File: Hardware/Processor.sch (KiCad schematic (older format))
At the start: 31 parts, among them J1 ICSP-CORTEX, J3 CONN-9, U6 STM32L100RBT6, U9 LM2903DT, X1 8MHz

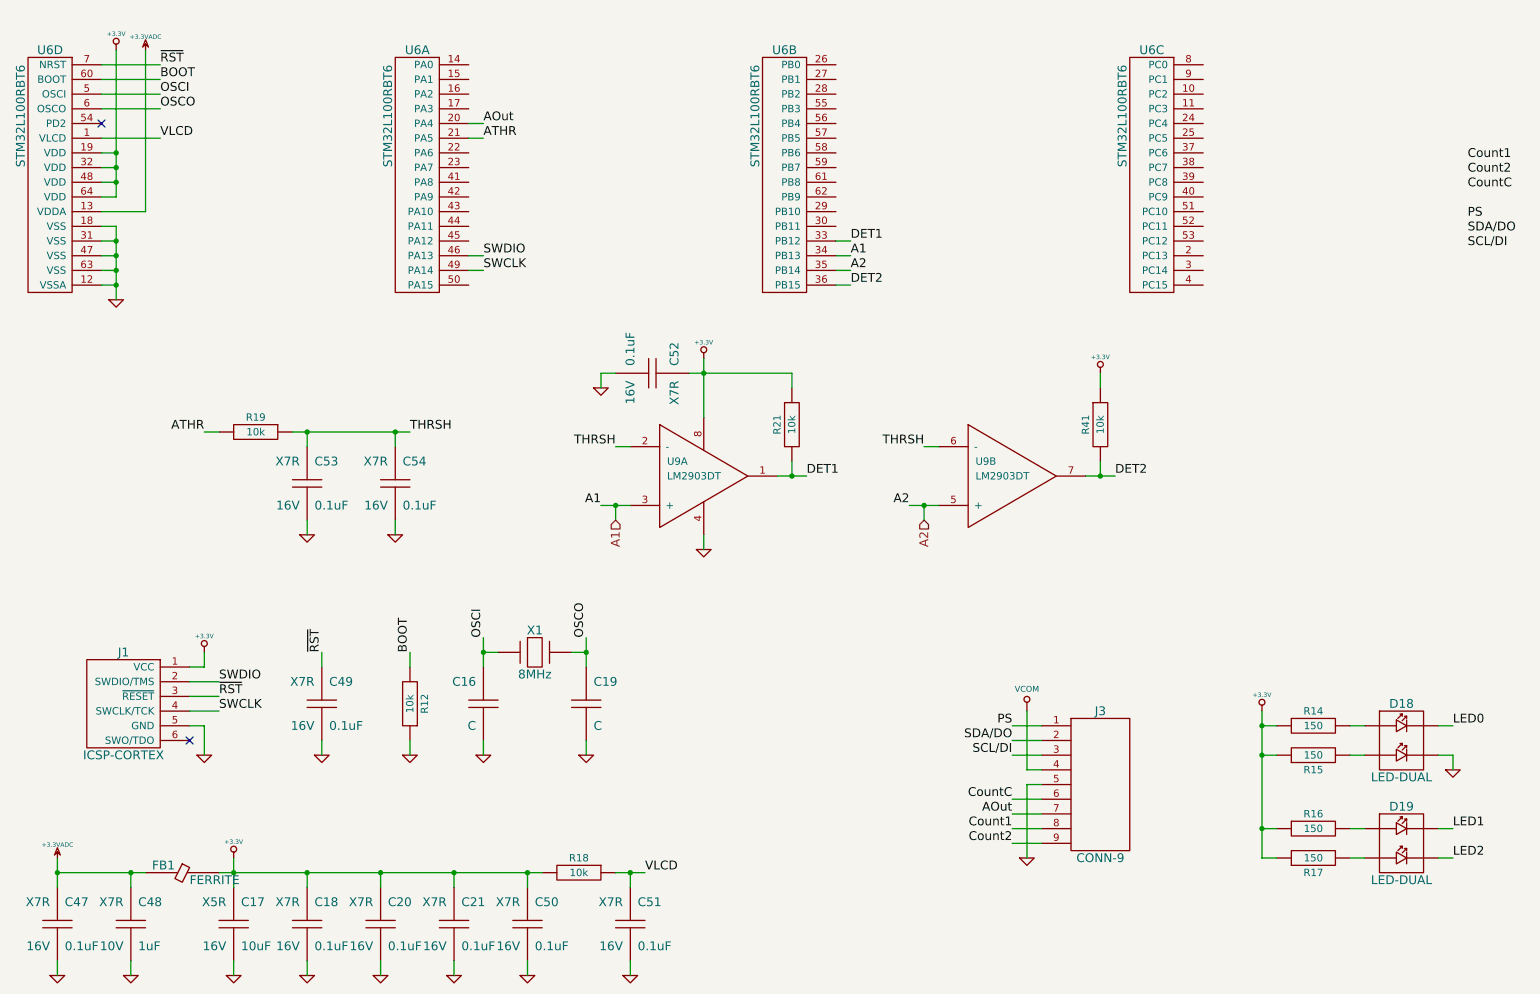
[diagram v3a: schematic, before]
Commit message: Serial IO connections
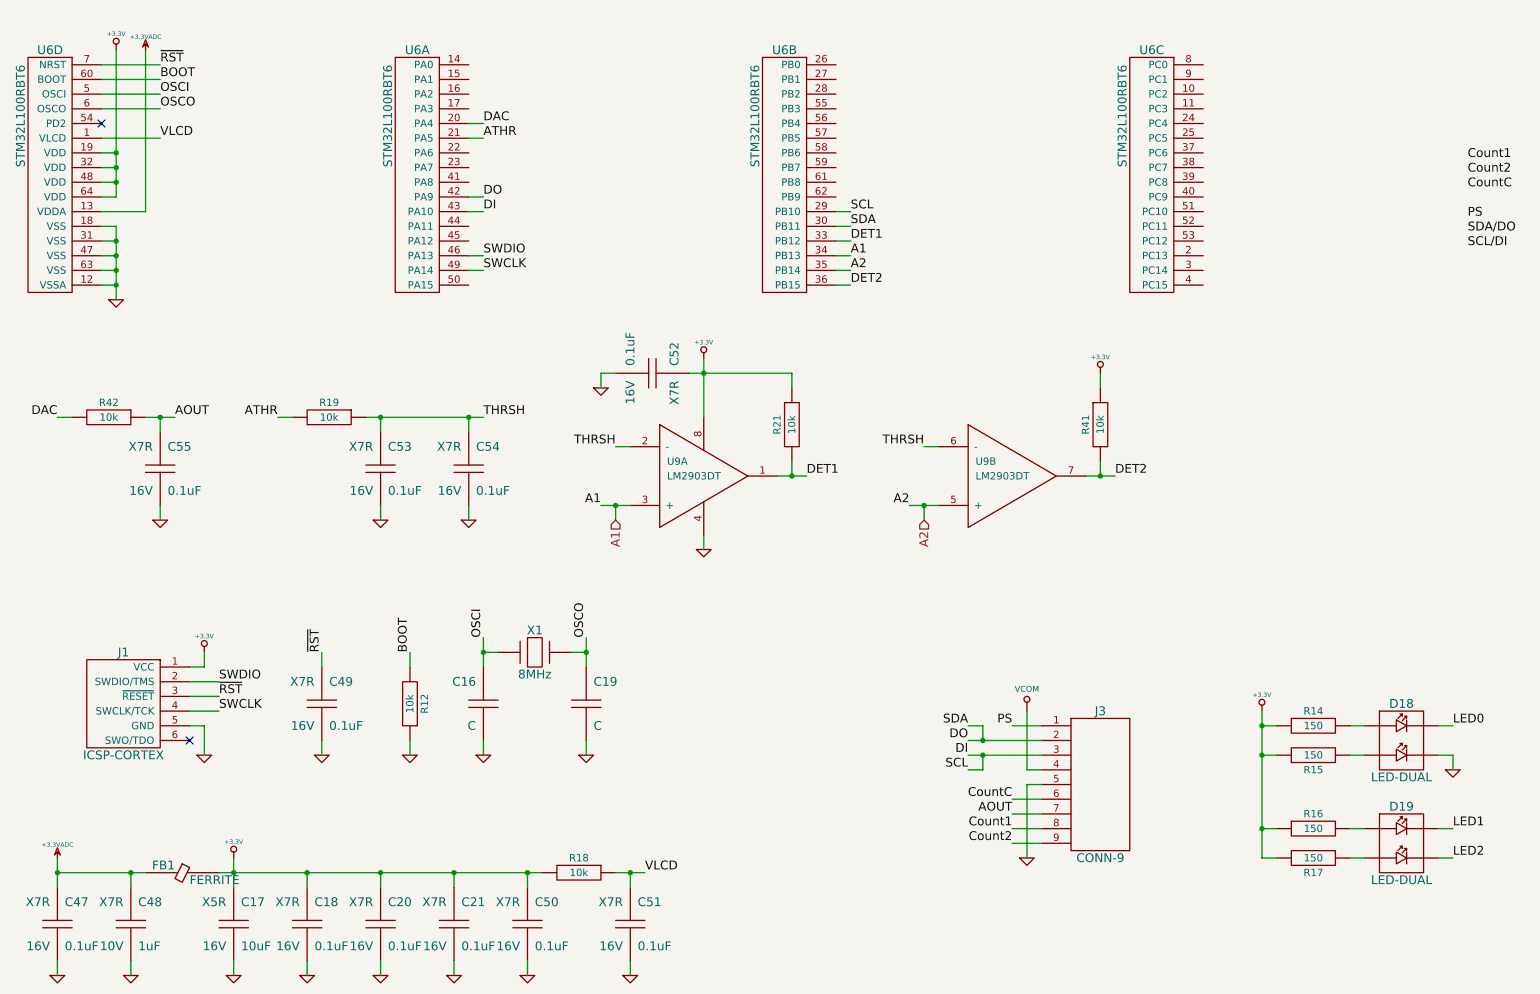
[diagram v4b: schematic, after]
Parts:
- added C55: 0.1uF, CAPC1608, symbol C
- added R42: 10k, RESC1608, symbol R
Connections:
- net GND: now also C55.2
- net SCL/DI: no longer J3.3
- net SDA/DO: no longer J3.2
- net DO: now reaches U6.42 (PA9)
- net DO: now also J3.2, U6.30 (PB11)
- net DI: now reaches U6.43 (PA10)
- net DI: now also J3.3, U6.29 (PB10)
- net AOut renamed AOUT
- net AOUT: now also C55.1, R42.1; no longer U6.20 (PA4)
- new net DAC: R42.2, U6.20 (PA4)
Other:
- moved on the sheet: C53, C54, R19
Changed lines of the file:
@@
 $EndComp
 $Comp
-L VCOM #PWR56
+L VCOM #PWR57
 U 1 1 52B50CC7
 P 7700 5400
-F 0 "#PWR56" H 7700 5600 40  0001 C CNN
+F 0 "#PWR57" H 7700 5600 40  0001 C CNN
 F 1 "VCOM" H 7700 5550 40  0000 C CNN
 F 2 "" H 7700 5400 60  0000 C CNN
@@
 	1    0    0    -1
 $EndComp
-Text Label 7600 5600 2    60   ~ 0
-SDA/DO
-Text Label 7600 5700 2    60   ~ 0
-SCL/DI
+Text Label 7300 5600 2    60   ~ 0
+DO
+Text Label 7300 5700 2    60   ~ 0
+DI
 $Comp
 L LED-DUAL D18
@@
 	7700 5800 7800 5800
 Wire Wire Line
-	7600 5600 7800 5600
-Wire Wire Line
-	7600 5700 7800 5700
+	7300 5600 7800 5600
+Wire Wire Line
+	7300 5700 7800 5700
 Wire Wire Line
 	10600 5800 10600 5700
@@
 	7600 5500 7800 5500
 Text Label 7600 6100 2    60   ~ 0
-AOut
+AOUT
 Wire Wire Line
 	7600 6100 7800 6100
@@
 CountC
 Text Label 4000 1400 0    60   ~ 0
-AOut
+DAC
 Text Label 10700 2050 0    60   ~ 0
 PS
@@
 Wire Wire Line
 	8200 3100 8200 3200
-Text Label 3500 3500 0    60   ~ 0
+Text Label 4000 3400 0    60   ~ 0
 THRSH
-Text Label 2100 3500 2    60   ~ 0
+Text Label 2600 3400 2    60   ~ 0
 ATHR
 Wire Wire Line
-	2100 3500 2200 3500
-Wire Wire Line
-	2700 3500 3500 3500
-Wire Wire Line
-	2800 3600 2800 3500
-Connection ~ 2800 3500
+	2600 3400 2700 3400
+Wire Wire Line
+	3200 3400 4000 3400
+Wire Wire Line
+	3300 3500 3300 3400
+Connection ~ 3300 3400
 $Comp
 L GND #PWR058
 U 1 1 54120E8C
-P 2800 4200
-F 0 "#PWR058" H 2800 4200 30  0001 C CNN
-F 1 "GND" H 2800 4130 30  0001 C CNN
-F 2 "" H 2800 4200 60  0000 C CNN
-F 3 "" H 2800 4200 60  0000 C CNN
-	1    2800 4200
-	1    0    0    -1
-$EndComp
-Wire Wire Line
-	2800 4200 2800 4100
+P 3300 4100
+F 0 "#PWR058" H 3300 4100 30  0001 C CNN
+F 1 "GND" H 3300 4030 30  0001 C CNN
+F 2 "" H 3300 4100 60  0000 C CNN
+F 3 "" H 3300 4100 60  0000 C CNN
+	1    3300 4100
+	1    0    0    -1
+$EndComp
+Wire Wire Line
+	3300 4100 3300 4000
 $Comp
 L C C53
 U 1 1 54120F9B
-P 2800 3850
-F 0 "C53" H 2850 4000 60  0000 L CNN
-F 1 "0.1uF" H 2850 3700 60  0000 L CNN
-F 2 "CAPC1608" H 2800 3850 60  0001 C CNN
-F 3 "~" H 2800 3850 60  0000 C CNN
-F 4 "Samsung" H 2800 3850 60  0001 C CNN "MFR Name"
-F 5 "CL10B104KO8NNNC" H 2800 3850 60  0001 C CNN "MFR Part No"
-F 6 "1276-1005-1-ND" H 2800 3850 60  0001 C CNN "Distributor Part No"
-F 7 "16V" H 2750 3700 60  0000 R CNN "Voltage"
-F 8 "X7R" H 2750 4000 60  0000 R CNN "Dielectric"
-	1    2800 3850
+P 3300 3750
+F 0 "C53" H 3350 3900 60  0000 L CNN
+F 1 "0.1uF" H 3350 3600 60  0000 L CNN
+F 2 "CAPC1608" H 3300 3750 60  0001 C CNN
+F 3 "~" H 3300 3750 60  0000 C CNN
+F 4 "Samsung" H 3300 3750 60  0001 C CNN "MFR Name"
+F 5 "CL10B104KO8NNNC" H 3300 3750 60  0001 C CNN "MFR Part No"
+F 6 "1276-1005-1-ND" H 3300 3750 60  0001 C CNN "Distributor Part No"
+F 7 "16V" H 3250 3600 60  0000 R CNN "Voltage"
+F 8 "X7R" H 3250 3900 60  0000 R CNN "Dielectric"
+	1    3300 3750
 	1    0    0    -1
 $EndComp
@@
 L R R19
 U 1 1 54120FD3
-P 2450 3500
-F 0 "R19" H 2450 3600 50  0000 C CNN
-F 1 "10k" H 2450 3500 50  0000 C CNN
-F 2 "RESC1608" H 2450 3500 60  0001 C CNN
-F 3 "~" H 2450 3500 60  0000 C CNN
-F 4 "Yageo" H 2450 3500 60  0001 C CNN "MFR Name"
-F 5 "RC0603FR-0710KL" H 2450 3500 60  0001 C CNN "MFR Part No"
-F 6 "311-10.0KHRCT-ND" H 2450 3500 60  0001 C CNN "Distributor Part No"
-F 7 "0.1W" H 2450 3400 50  0001 C CNN "Power"
-F 8 "1%" H 2450 3300 50  0001 C CNN "Tolerance"
-	1    2450 3500
+P 2950 3400
+F 0 "R19" H 2950 3500 50  0000 C CNN
+F 1 "10k" H 2950 3400 50  0000 C CNN
+F 2 "RESC1608" H 2950 3400 60  0001 C CNN
+F 3 "~" H 2950 3400 60  0000 C CNN
+F 4 "Yageo" H 2950 3400 60  0001 C CNN "MFR Name"
+F 5 "RC0603FR-0710KL" H 2950 3400 60  0001 C CNN "MFR Part No"
+F 6 "311-10.0KHRCT-ND" H 2950 3400 60  0001 C CNN "Distributor Part No"
+F 7 "0.1W" H 2950 3300 50  0001 C CNN "Power"
+F 8 "1%" H 2950 3200 50  0001 C CNN "Tolerance"
+	1    2950 3400
 	-1   0    0    -1
 $EndComp
@@
 L C C54
 U 1 1 541211F5
-P 3400 3850
-F 0 "C54" H 3450 4000 60  0000 L CNN
-F 1 "0.1uF" H 3450 3700 60  0000 L CNN
-F 2 "CAPC1608" H 3400 3850 60  0001 C CNN
-F 3 "~" H 3400 3850 60  0000 C CNN
-F 4 "Samsung" H 3400 3850 60  0001 C CNN "MFR Name"
-F 5 "CL10B104KO8NNNC" H 3400 3850 60  0001 C CNN "MFR Part No"
-F 6 "1276-1005-1-ND" H 3400 3850 60  0001 C CNN "Distributor Part No"
-F 7 "16V" H 3350 3700 60  0000 R CNN "Voltage"
-F 8 "X7R" H 3350 4000 60  0000 R CNN "Dielectric"
-	1    3400 3850
-	1    0    0    -1
-$EndComp
-Wire Wire Line
-	3400 3600 3400 3500
-Connection ~ 3400 3500
+P 3900 3750
+F 0 "C54" H 3950 3900 60  0000 L CNN
+F 1 "0.1uF" H 3950 3600 60  0000 L CNN
+F 2 "CAPC1608" H 3900 3750 60  0001 C CNN
+F 3 "~" H 3900 3750 60  0000 C CNN
+F 4 "Samsung" H 3900 3750 60  0001 C CNN "MFR Name"
+F 5 "CL10B104KO8NNNC" H 3900 3750 60  0001 C CNN "MFR Part No"
+F 6 "1276-1005-1-ND" H 3900 3750 60  0001 C CNN "Distributor Part No"
+F 7 "16V" H 3850 3600 60  0000 R CNN "Voltage"
+F 8 "X7R" H 3850 3900 60  0000 R CNN "Dielectric"
+	1    3900 3750
+	1    0    0    -1
+$EndComp
+Wire Wire Line
+	3900 3500 3900 3400
+Connection ~ 3900 3400
 $Comp
 L GND #PWR059
 U 1 1 541212A0
-P 3400 4200
-F 0 "#PWR059" H 3400 4200 30  0001 C CNN
-F 1 "GND" H 3400 4130 30  0001 C CNN
-F 2 "" H 3400 4200 60  0000 C CNN
-F 3 "" H 3400 4200 60  0000 C CNN
-	1    3400 4200
-	1    0    0    -1
-$EndComp
-Wire Wire Line
-	3400 4200 3400 4100
+P 3900 4100
+F 0 "#PWR059" H 3900 4100 30  0001 C CNN
+F 1 "GND" H 3900 4030 30  0001 C CNN
+F 2 "" H 3900 4100 60  0000 C CNN
+F 3 "" H 3900 4100 60  0000 C CNN
+	1    3900 4100
+	1    0    0    -1
+$EndComp
+Wire Wire Line
+	3900 4100 3900 4000
+$Comp
+L R R42
+U 1 1 54121756
+P 1450 3400
+F 0 "R42" H 1450 3500 50  0000 C CNN
+F 1 "10k" H 1450 3400 50  0000 C CNN
+F 2 "RESC1608" H 1450 3400 60  0001 C CNN
+F 3 "~" H 1450 3400 60  0000 C CNN
+F 4 "Yageo" H 1450 3400 60  0001 C CNN "MFR Name"
+F 5 "RC0603FR-0710KL" H 1450 3400 60  0001 C CNN "MFR Part No"
+F 6 "311-10.0KHRCT-ND" H 1450 3400 60  0001 C CNN "Distributor Part No"
+F 7 "0.1W" H 1450 3300 50  0001 C CNN "Power"
+F 8 "1%" H 1450 3200 50  0001 C CNN "Tolerance"
+	1    1450 3400
+	-1   0    0    -1
+$EndComp
+$Comp
+L C C55
+U 1 1 54121761
+P 1800 3750
+F 0 "C55" H 1850 3900 60  0000 L CNN
+F 1 "0.1uF" H 1850 3600 60  0000 L CNN
+F 2 "CAPC1608" H 1800 3750 60  0001 C CNN
+F 3 "~" H 1800 3750 60  0000 C CNN
+F 4 "Samsung" H 1800 3750 60  0001 C CNN "MFR Name"
+F 5 "CL10B104KO8NNNC" H 1800 3750 60  0001 C CNN "MFR Part No"
+F 6 "1276-1005-1-ND" H 1800 3750 60  0001 C CNN "Distributor Part No"
+F 7 "16V" H 1750 3600 60  0000 R CNN "Voltage"
+F 8 "X7R" H 1750 3900 60  0000 R CNN "Dielectric"
+	1    1800 3750
+	1    0    0    -1
+$EndComp
+Text Label 1900 3400 0    60   ~ 0
+AOUT
+Text Label 1100 3400 2    60   ~ 0
+DAC
+Wire Wire Line
+	1100 3400 1200 3400
+Wire Wire Line
+	1700 3400 1900 3400
+Wire Wire Line
+	1800 3500 1800 3400
+Connection ~ 1800 3400
+$Comp
+L GND #PWR060
+U 1 1 5412190A
+P 1800 4100
+F 0 "#PWR060" H 1800 4100 30  0001 C CNN
+F 1 "GND" H 1800 4030 30  0001 C CNN
+F 2 "" H 1800 4100 60  0000 C CNN
+F 3 "" H 1800 4100 60  0000 C CNN
+	1    1800 4100
+	1    0    0    -1
+$EndComp
+Wire Wire Line
+	1800 4100 1800 4000
+Text Label 4000 1900 0    60   ~ 0
+DO
+Text Label 4000 2000 0    60   ~ 0
+DI
+Wire Wire Line
+	3900 1900 4000 1900
+Wire Wire Line
+	4000 2000 3900 2000
+Text Label 6500 2000 0    60   ~ 0
+SCL
+Text Label 6500 2100 0    60   ~ 0
+SDA
+Wire Wire Line
+	6500 2000 6400 2000
+Wire Wire Line
+	6500 2100 6400 2100
+Text Label 7300 5500 2    60   ~ 0
+SDA
+Wire Wire Line
+	7300 5500 7400 5500
+Wire Wire Line
+	7400 5500 7400 5600
+Connection ~ 7400 5600
+Text Label 7300 5800 2    60   ~ 0
+SCL
+Wire Wire Line
+	7300 5800 7400 5800
+Wire Wire Line
+	7400 5800 7400 5700
+Connection ~ 7400 5700
 $EndSCHEMATC

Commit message: EDRC checking
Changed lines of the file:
@@
 L VCOM #PWR57
 U 1 1 52B50CC7
-P 7700 5400
-F 0 "#PWR57" H 7700 5600 40  0001 C CNN
-F 1 "VCOM" H 7700 5550 40  0000 C CNN
-F 2 "" H 7700 5400 60  0000 C CNN
-F 3 "" H 7700 5400 60  0000 C CNN
-	1    7700 5400
+P 7700 5300
+F 0 "#PWR57" H 7700 5500 40  0001 C CNN
+F 1 "VCOM" H 7700 5450 40  0000 C CNN
+F 2 "" H 7700 5300 60  0000 C CNN
+F 3 "" H 7700 5300 60  0000 C CNN
+	1    7700 5300
 	1    0    0    -1
 $EndComp
@@
 	7700 5900 7800 5900
 Wire Wire Line
-	7700 5400 7700 5800
+	7700 5300 7700 5800
 Wire Wire Line
 	7700 5800 7800 5800
@@
 Connection ~ 2300 6500
 Wire Wire Line
-	1600 6600 1600 6500
+	1600 6400 1600 6600
 Connection ~ 1600 6500
 Wire Wire Line
@@
 	4900 6500 5100 6500
 Wire Wire Line
-	5000 6500 5000 6600
+	5000 6400 5000 6600
 $Comp
 L GND #PWR047
@@
 	7400 5800 7400 5700
 Connection ~ 7400 5700
+$Comp
+L PWR_FLAG #FLG061
+U 1 1 5412220A
+P 1600 6400
+F 0 "#FLG061" H 1600 6495 30  0001 C CNN
+F 1 "PWR_FLAG" H 1600 6580 30  0000 C CNN
+F 2 "" H 1600 6400 60  0000 C CNN
+F 3 "" H 1600 6400 60  0000 C CNN
+	1    1600 6400
+	1    0    0    -1
+$EndComp
+$Comp
+L PWR_FLAG #FLG062
+U 1 1 541222E3
+P 5000 6400
+F 0 "#FLG062" H 5000 6495 30  0001 C CNN
+F 1 "PWR_FLAG" H 5000 6580 30  0000 C CNN
+F 2 "" H 5000 6400 60  0000 C CNN
+F 3 "" H 5000 6400 60  0000 C CNN
+	1    5000 6400
+	1    0    0    -1
+$EndComp
+$Comp
+L PWR_FLAG #FLG063
+U 1 1 54122476
+P 7900 5300
+F 0 "#FLG063" H 7900 5395 30  0001 C CNN
+F 1 "PWR_FLAG" H 7900 5480 30  0000 C CNN
+F 2 "" H 7900 5300 60  0000 C CNN
+F 3 "" H 7900 5300 60  0000 C CNN
+	1    7900 5300
+	1    0    0    -1
+$EndComp
+Wire Wire Line
+	7900 5300 7900 5400
+Wire Wire Line
+	7900 5400 7700 5400
+Connection ~ 7700 5400
 $EndSCHEMATC

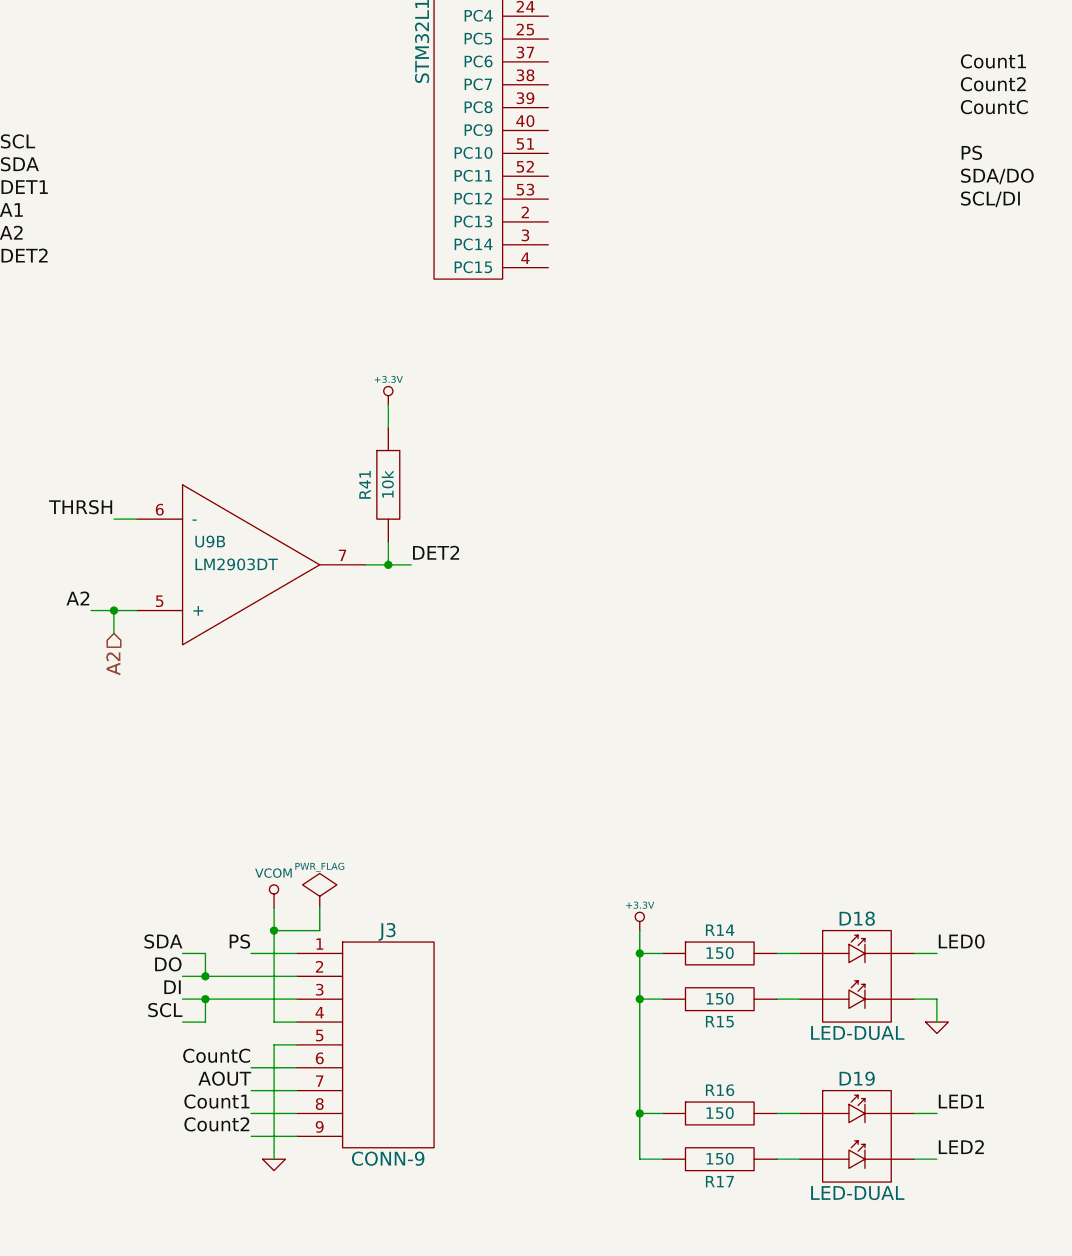
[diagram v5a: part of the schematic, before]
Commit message: Change output pinout
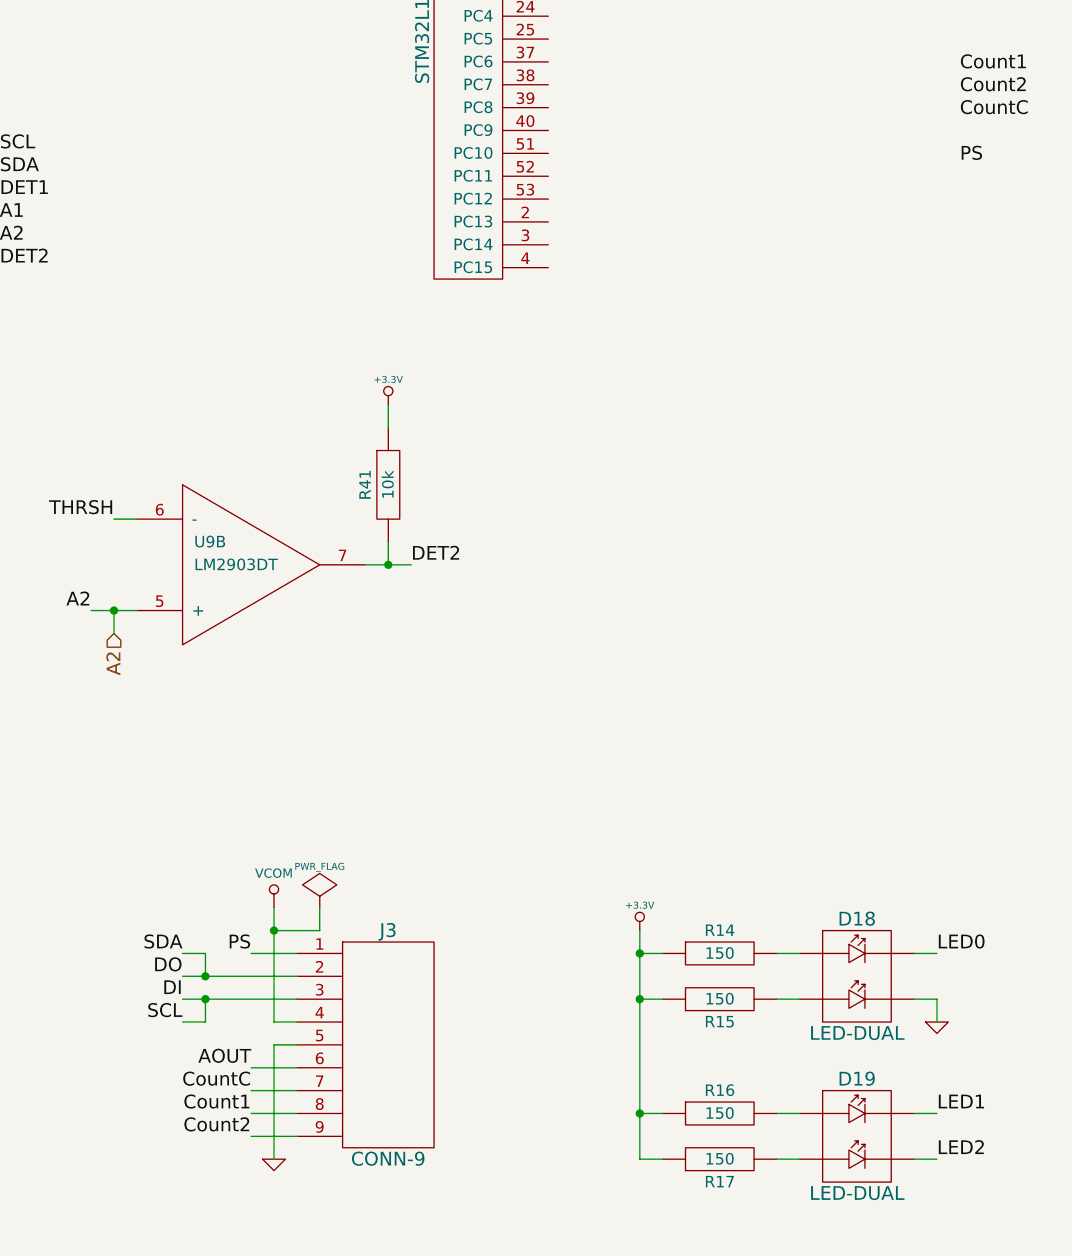
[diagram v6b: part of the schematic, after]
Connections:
- net AOUT: now also J3.6; no longer J3.7
- net CountC: now also J3.7; no longer J3.6
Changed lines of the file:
@@
 Wire Wire Line
 	7600 6300 7800 6300
-Text Label 7600 6000 2    60   ~ 0
+Text Label 7600 6100 2    60   ~ 0
 CountC
 Wire Wire Line
@@
 Wire Wire Line
 	7600 5500 7800 5500
-Text Label 7600 6100 2    60   ~ 0
+Text Label 7600 6000 2    60   ~ 0
 AOUT
 Wire Wire Line
@@
 Text Label 10700 2050 0    60   ~ 0
 PS
-Text Label 10700 2150 0    60   ~ 0
-SDA/DO
-Text Label 10700 2250 0    60   ~ 0
-SCL/DI
 $Comp
 L ICSP-CORTEX J1
